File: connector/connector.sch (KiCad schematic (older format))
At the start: 6 parts, among them J1 Conn_01x04_Female, J2 Conn_01x04

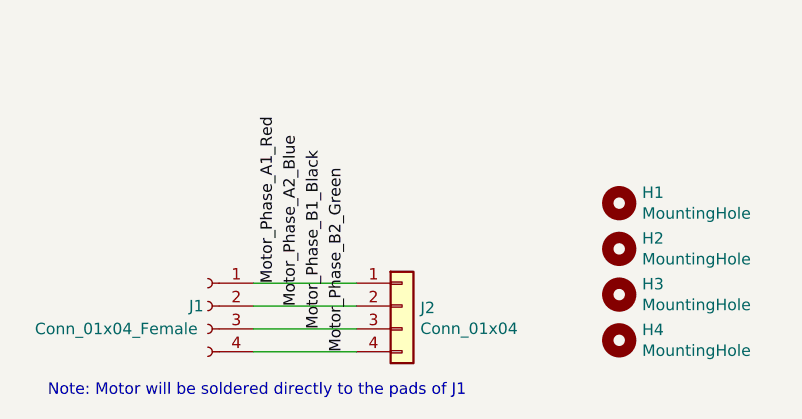
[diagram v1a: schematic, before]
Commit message: Updated BOM with final cap counts and symbol names
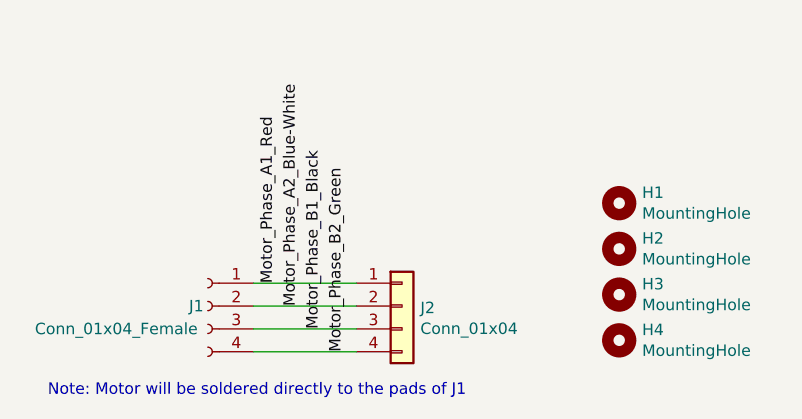
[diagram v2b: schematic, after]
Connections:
- net Motor_Phase_A2_Blue renamed Motor_Phase_A2_Blue-White
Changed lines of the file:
@@
 Motor_Phase_A1_Red
 Text Label 5750 3800 1    50   ~ 0
-Motor_Phase_A2_Blue
+Motor_Phase_A2_Blue-White
 Text Label 5850 3900 1    50   ~ 0
 Motor_Phase_B1_Black
